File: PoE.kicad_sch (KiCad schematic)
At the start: 33 parts

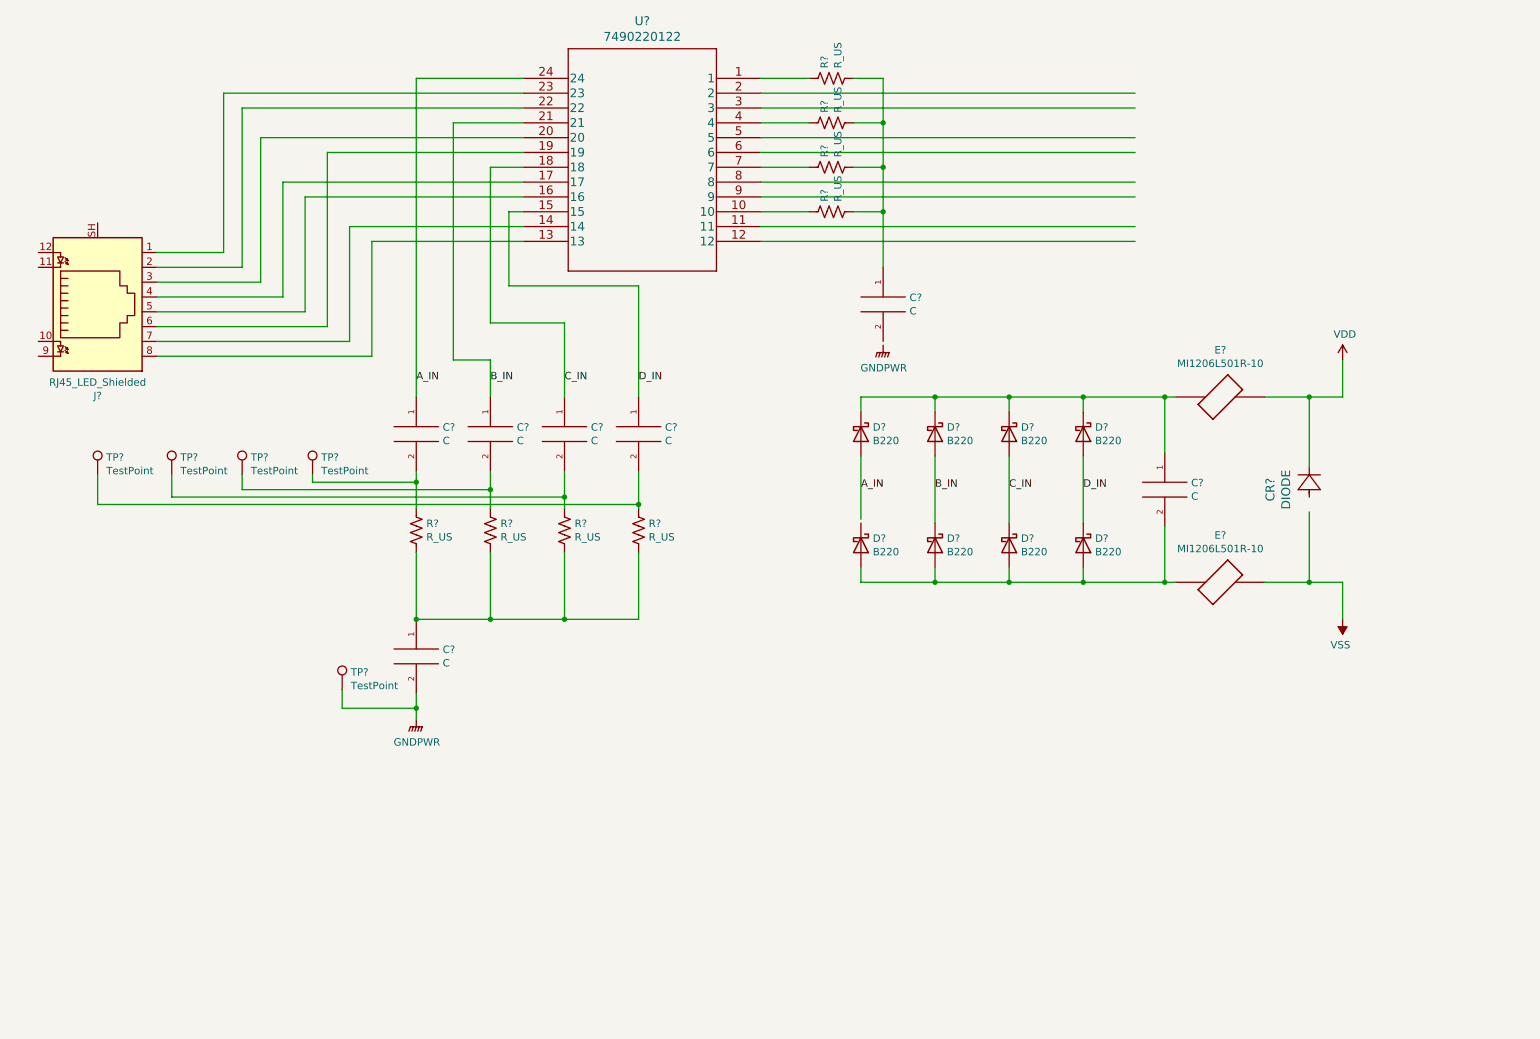
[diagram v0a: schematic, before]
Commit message: Added sheet for flyback
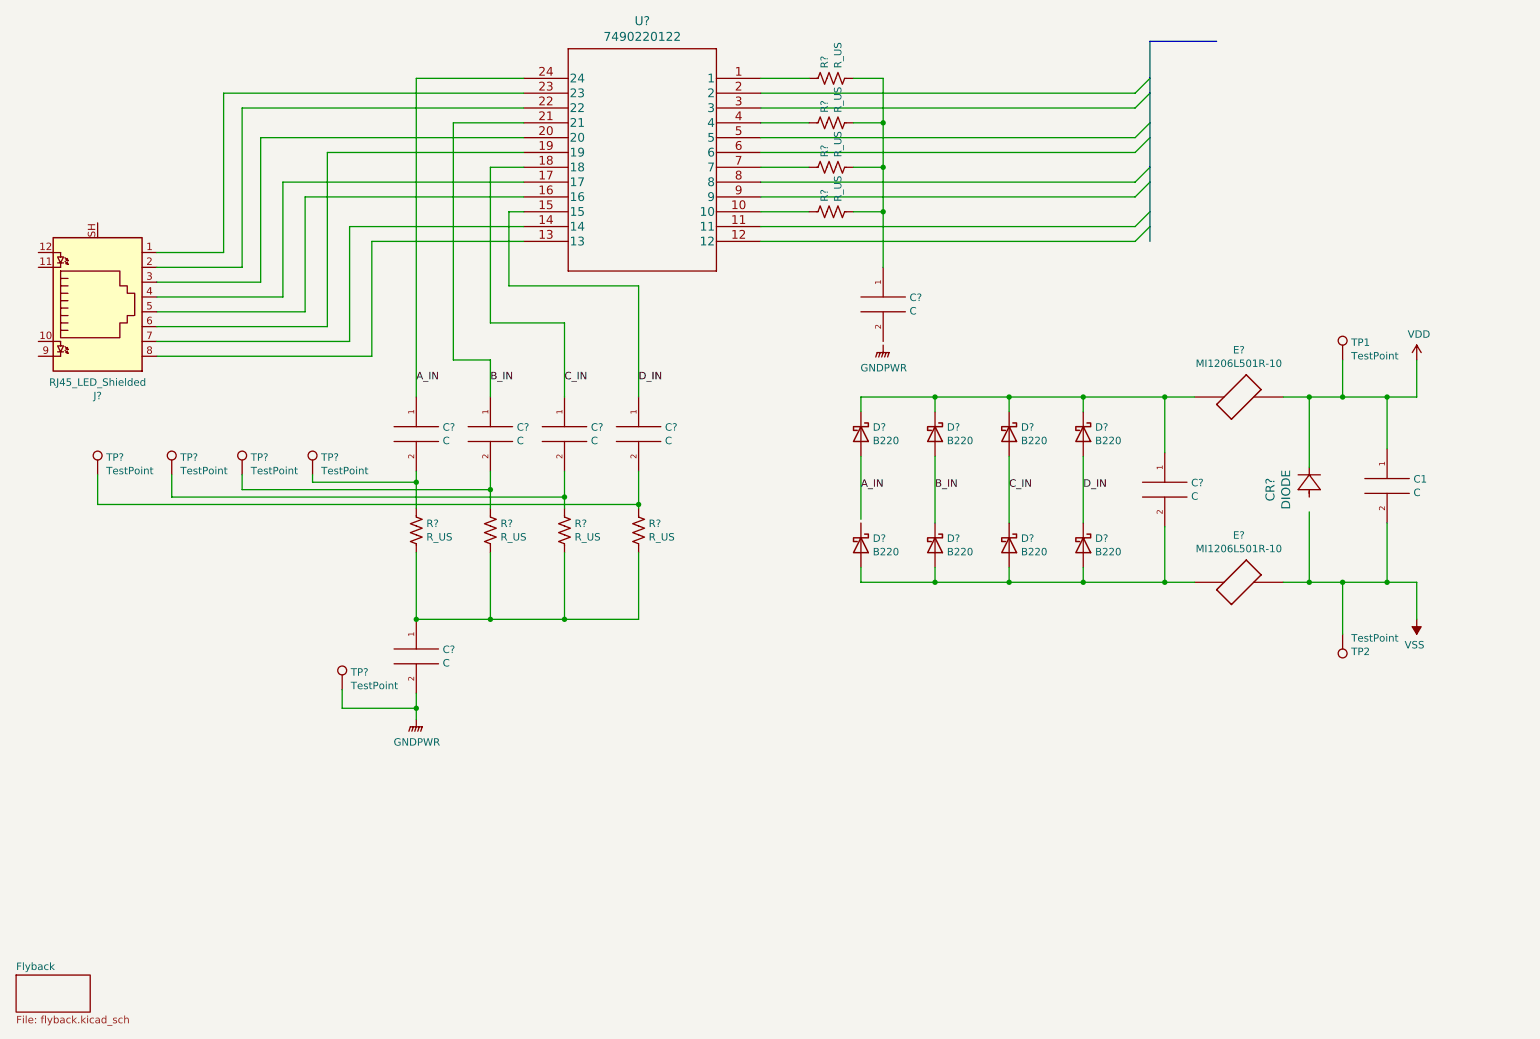
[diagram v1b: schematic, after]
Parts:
- added C1: C, symbol PoE-rescue:C-pspice
- added TP1, TP2: TestPoint, symbol Connector:TestPoint
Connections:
- net VDD: now also C1.1, TP1.1
- net VSS: now also C1.2, TP2.1
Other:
- added sheet Flyback (flyback.kicad_sch)
- moved on the sheet: E?

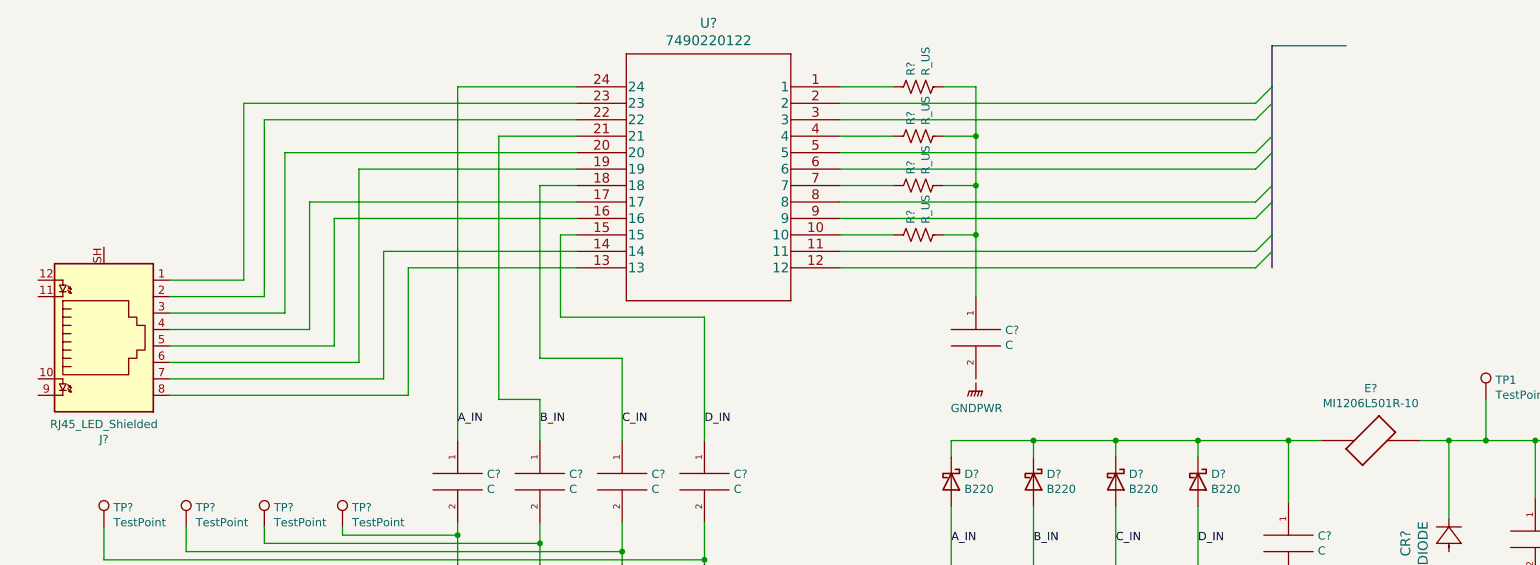
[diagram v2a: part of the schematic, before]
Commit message: More updates, added bus
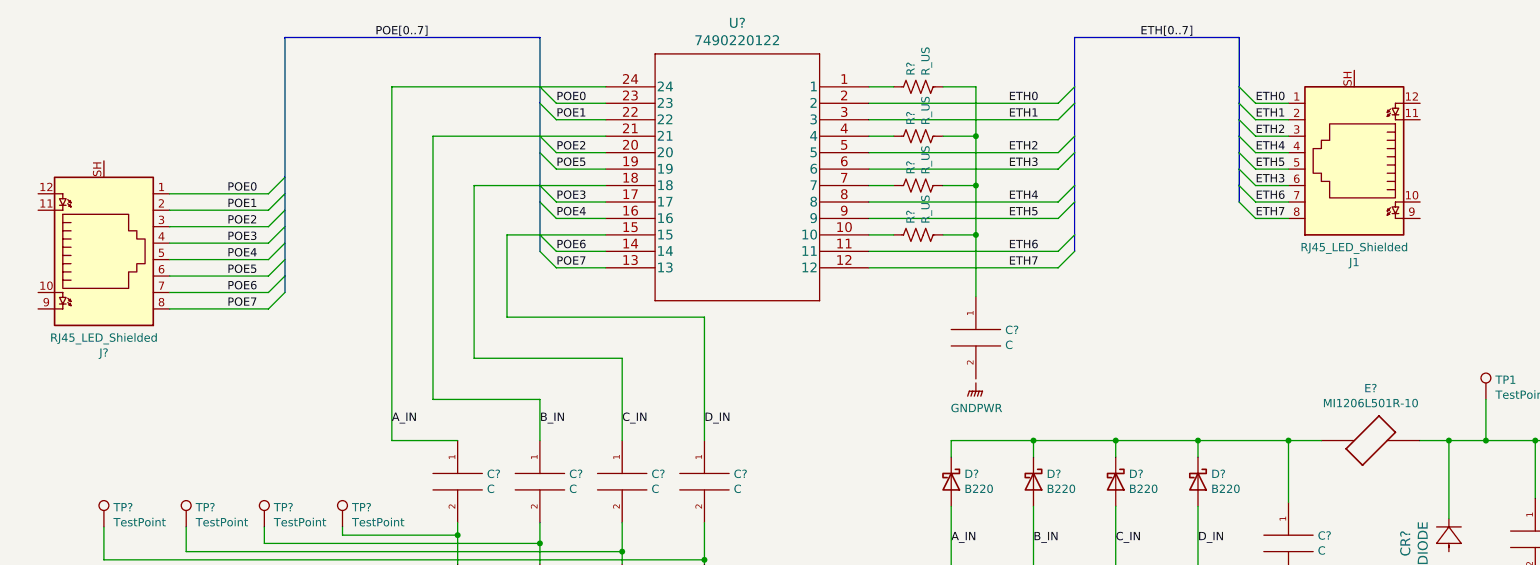
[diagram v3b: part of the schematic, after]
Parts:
- added J1: RJ45_LED_Shielded, symbol Connector:RJ45_LED_Shielded
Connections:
- net ETH6: now reaches U?.11
- net ETH6: now also J1.7
- net ETH7: now reaches U?.12
- net ETH7: now also J1.8
- net POE7: now reaches J?.8, U?.13
- net POE6: now reaches J?.7, U?.14
- net POE4: now reaches J?.5, U?.16
- net POE3: now reaches J?.4, U?.17
- net POE5: now reaches J?.6, U?.19
- net ETH0: now reaches U?.2
- net ETH0: now also J1.1
- net POE2: now reaches J?.3, U?.20
- net POE1: now reaches J?.2, U?.22
- net POE0: now reaches J?.1, U?.23
- net ETH1: now reaches U?.3
- net ETH1: now also J1.2
- net ETH2: now reaches U?.5
- net ETH2: now also J1.3
- net ETH3: now reaches U?.6
- net ETH3: now also J1.6
- net ETH4: now reaches U?.8
- net ETH4: now also J1.4
- net ETH5: now reaches U?.9
- net ETH5: now also J1.5
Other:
- moved on the sheet: J?, U?

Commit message: Minor updates and adding footprints
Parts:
- removed CR?: DIODE, SMASeries_LTF, symbol PoE-rescue:DIODE-SMAJ58A
- removed E? (x2): MI1206L501R-10, FB_MI1206L501R-10, symbol PoE-rescue:MI1206L501R-10-MI1206L501R-10
- removed J1, J?: RJ45_LED_Shielded, symbol Connector:RJ45_LED_Shielded
- added D109: SMAJ58A, Diode_SMD:D_SMA, symbol Diode:SMAJ58A
- added J101, J102: ARJM11B1-009-AB-EW2, footprints:CONN12_ARJM11B1-009-AB-EW2_ABR, symbol ARJM11B1_009_AB_EW2:ARJM11B1-009-AB-EW2
- C101, C107, C108: renamed from C?; value C -> 1n; footprint (none) -> SparkFun-Capacitor:C_0402_1005Metric
- C102, C103, C104, C105: renamed from C?; value C -> 10n; footprint (none) -> SparkFun-Capacitor:C_0402_1005Metric
- C106: renamed from C1; value C -> 100n; footprint (none) -> SparkFun-Capacitor:C_0402_1005Metric
- R101, R102, R103, R104, R105, R106, R107, R108: renamed from R?; value R_US -> 75; footprint (none) -> Resistor_SMD:R_01005_0402Metric
- TP101: renamed from TP1; footprint (none) -> SparkFun-Connector:TestPoint-1.0mm
- TP102, TP103, TP104, TP105, TP107: renamed from TP?; footprint (none) -> SparkFun-Connector:TestPoint-1.0mm
- TP106: renamed from TP2; footprint (none) -> SparkFun-Connector:TestPoint-1.0mm
- U101: renamed from U?; footprint 7490220122_WRE -> Transformer_SMD:Transformer_Ethernet_Wuerth_749013011A
- gave numbers to parts that had none: 8
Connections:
- net ETH0: now also J102.1
- net ETH1: now also J102.2
- net ETH2: now also J102.3
- net ETH3: now also J102.6
- net ETH4: now also J102.4
- net ETH5: now also J102.5
- net ETH6: now also J102.7
- net ETH7: now also J102.8
- net POE0: now also J101.1
- net POE1: now also J101.2
- net POE2: now also J101.3
- net POE3: now also J101.4
- net POE4: now also J101.5
- net POE5: now also J101.6
- net POE6: now also J101.7
- net POE7: now also J101.8
- net VDD: now also D109.1 (A1)
- net VSS: now also D109.2 (A2)
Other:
- moved on the sheet: C101, R101, R102, R103, R104

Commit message: Found footprints
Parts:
- added D1010: LED, LED_SMD:LED_0402_1005Metric, symbol Device:LED
- added FB1001, FB1002: FerriteBead, Resistor_SMD:R_0805_2012Metric, symbol Device:FerriteBead
- added R1009: 24.9k, Resistor_SMD:R_0402_1005Metric, symbol Device:R_US
- added R1010: 2.2k, Resistor_SMD:R_0402_1005Metric, symbol Device:R_US
- added U1002: TCMT1107, footprints:SSOP4_4P40X2P85_VIS, symbol TCMT1107:TCMT1107
- renumbered C101 to C1001, C102 to C1002, C103 to C1003, C104 to C1004, C105 to C1005, C106 to C1006, C107 to C1007, C108 to C1008, D101 to D1001, D102 to D1002, D103 to D1003, D104 to D1004, D109 to D1005, D105 to D1006, D106 to D1007, D107 to D1008, D108 to D1009, J102 to J1001, J101 to J1002, R101 to R1001, R102 to R1002, R103 to R1003, R104 to R1004, R105 to R1005, R106 to R1006, R107 to R1007, R108 to R1008, TP101 to TP1001, TP102 to TP1002, TP103 to TP1003, TP104 to TP1004, TP105 to TP1005, TP106 to TP1006, TP107 to TP1007, U101 to U1001
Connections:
- net VDD: now also FB1001.1
- net VSS: now also FB1002.1
- net at C1007.1, D1001.1 (K), D1002.1 (K)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: now also FB1001.2
- net at C1007.2, D1006.2 (A), D1007.2 (A)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: now also FB1002.2
- new net: R1009.2, U1002.1 (A)
- new net: R1010.2, U1002.4 (C)
- new net: D1010.1 (K), R1010.1
- new net +5V: D1010.2 (A)
- new net GNDREF: U1002.3 (E)
- new net T2P: U1002.2 (C)
- new net VC: R1009.1
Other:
- moved on the sheet: C1006, D1005, TP1001, TP1006

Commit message: Updating layout
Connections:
- net A_IN: now also D1006.1 (K)
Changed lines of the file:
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@@
+	(wire
+		(pts
+			(xy 171.45 92.71) (xy 171.45 104.14)
+		)
+		(stroke
+			(width 0)
+			(type default)
+		)
+	)
 	(wire
 		(pts
@@
 		)
 		(stroke
-			(width 0)
-			(type default)
-		)
-	)
-	(wire
-		(pts
-			(xy 171.45 103.505) (xy 171.45 92.71)
-		)
-		(stroke

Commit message: Changed all passive footprints to 0805
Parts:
- C1001, C1002, C1003, C1004, C1005, C1006, C1007, C1008: footprint SparkFun-Capacitor:C_0402_1005Metric -> Capacitor_SMD:C_0805_2012Metric
- R1001, R1002, R1003, R1004, R1005, R1006, R1007, R1008: footprint Resistor_SMD:R_01005_0402Metric -> Resistor_SMD:R_0805_2012Metric
- R1009, R1010: footprint Resistor_SMD:R_0402_1005Metric -> Resistor_SMD:R_0805_2012Metric
- U1001: footprint Transformer_SMD:Transformer_Ethernet_Wuerth_749013011A -> footprints:7490220122
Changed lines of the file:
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@@
 			)
 		)
-		(property "Footprint" "Transformer_SMD:Transformer_Ethernet_Wuerth_749013011A"
+		(property "Footprint" "footprints:7490220122"
 			(at 138.43 21.844 0)
 			(effects
@@
 			)
 		)
-		(property "Footprint" "SparkFun-Capacitor:C_0402_1005Metric"
+		(property "Footprint" "Capacitor_SMD:C_0805_2012Metric"
 			(at 95.25 88.9 0)
 			(effects
@@
 			)
 		)
-		(property "Footprint" "SparkFun-Capacitor:C_0402_1005Metric"
+		(property "Footprint" "Capacitor_SMD:C_0805_2012Metric"
 			(at 107.95 88.9 0)
 			(effects
@@
 			)
 		)
-		(property "Footprint" "SparkFun-Capacitor:C_0402_1005Metric"
+		(property "Footprint" "Capacitor_SMD:C_0805_2012Metric"
 			(at 120.65 88.9 0)
 			(effects
@@
 			)
 		)
-		(property "Footprint" "SparkFun-Capacitor:C_0402_1005Metric"
+		(property "Footprint" "Capacitor_SMD:C_0805_2012Metric"
 			(at 133.35 88.9 0)
 			(effects
@@
 			)
 		)
-		(property "Footprint" "Resistor_SMD:R_01005_0402Metric"
+		(property "Footprint" "Resistor_SMD:R_0805_2012Metric"
 			(at 96.266 105.664 90)
 			(effects
@@
 			)
 		)
-		(property "Footprint" "Resistor_SMD:R_01005_0402Metric"
+		(property "Footprint" "Resistor_SMD:R_0805_2012Metric"
 			(at 108.966 105.664 90)
 			(effects
@@
 			)
 		)
-		(property "Footprint" "Resistor_SMD:R_01005_0402Metric"
+		(property "Footprint" "Resistor_SMD:R_0805_2012Metric"
 			(at 121.666 105.664 90)
 			(effects
@@
 			)
 		)
-		(property "Footprint" "Resistor_SMD:R_01005_0402Metric"
+		(property "Footprint" "Resistor_SMD:R_0805_2012Metric"
 			(at 134.366 105.664 90)
 			(effects
@@
 			)
 		)
-		(property "Footprint" "SparkFun-Capacitor:C_0402_1005Metric"
+		(property "Footprint" "Capacitor_SMD:C_0805_2012Metric"
 			(at 95.25 127 0)
 			(effects
@@
 			)
 		)
-		(property "Footprint" "Resistor_SMD:R_01005_0402Metric"
+		(property "Footprint" "Resistor_SMD:R_0805_2012Metric"
 			(at 198.374 26.924 90)
 			(effects
@@
 			)
 		)
-		(property "Footprint" "Resistor_SMD:R_01005_0402Metric"
+		(property "Footprint" "Resistor_SMD:R_0805_2012Metric"
 			(at 198.374 34.544 90)
 			(effects
@@
 			)
 		)
-		(property "Footprint" "Resistor_SMD:R_01005_0402Metric"
+		(property "Footprint" "Resistor_SMD:R_0805_2012Metric"
 			(at 198.374 42.164 90)
 			(effects
@@
 			)
 		)
-		(property "Footprint" "Resistor_SMD:R_01005_0402Metric"
+		(property "Footprint" "Resistor_SMD:R_0805_2012Metric"
 			(at 198.374 49.784 90)
 			(effects
@@
 			)
 		)
-		(property "Footprint" "SparkFun-Capacitor:C_0402_1005Metric"
+		(property "Footprint" "Capacitor_SMD:C_0805_2012Metric"
 			(at 207.01 66.675 0)
 			(effects
@@
 			)
 		)
-		(property "Footprint" "SparkFun-Capacitor:C_0402_1005Metric"
+		(property "Footprint" "Capacitor_SMD:C_0805_2012Metric"
 			(at 223.52 98.425 0)
 			(effects
@@
 			)
 		)
-		(property "Footprint" "SparkFun-Capacitor:C_0402_1005Metric"
+		(property "Footprint" "Capacitor_SMD:C_0805_2012Metric"
 			(at 274.32 97.79 0)
 			(effects
@@
 			)
 		)
-		(property "Footprint" "Resistor_SMD:R_0402_1005Metric"
+		(property "Footprint" "Resistor_SMD:R_0805_2012Metric"
 			(at 78.486 165.354 90)
 			(effects
@@
 			)
 		)
-		(property "Footprint" "Resistor_SMD:R_0402_1005Metric"
+		(property "Footprint" "Resistor_SMD:R_0805_2012Metric"
 			(at 127.254 169.164 90)
 			(effects

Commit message: Starting Layout
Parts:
- removed J1001, J1002: ARJM11B1-009-AB-EW2, footprints:CONN12_ARJM11B1-009-AB-EW2_ABR, symbol ARJM11B1_009_AB_EW2:ARJM11B1-009-AB-EW2
- added J1001, J1002: 8P8C_LED_Shielded_x2, footprints:CONN12_ARJM11B1-009-AB-EW2_ABR, symbol Connector:8P8C_LED_Shielded_x2
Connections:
- net ETH0: now also J1001.1
- net ETH1: now also J1001.2
- net ETH2: now also J1001.3
- net ETH3: now also J1001.6
- net ETH4: now also J1001.4
- net ETH5: now also J1001.5
- net ETH6: now also J1001.7
- net ETH7: now also J1001.8
- net GNDPWR: now also J1002.SH
- net GNDREF: now also J1001.SH
- net POE0: now also J1002.1
- net POE1: now also J1002.2
- net POE2: now also J1002.3
- net POE3: now also J1002.4
- net POE4: now also J1002.5
- net POE5: now also J1002.6
- net POE6: now also J1002.7
- net POE7: now also J1002.8
